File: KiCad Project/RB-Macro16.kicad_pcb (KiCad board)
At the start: 2 copper layers, 3.4 x 3 mm, 67 parts, among them J1 USB_C_Receptacle, J2 AVR-ISP-6, K0A1 KEYSW, K0B1 KEYSW, K0C1 KEYSW, K0D1 KEYSW, K1A1 KEYSW, K1B1 KEYSW, K1C1 KEYSW, K1D1 KEYSW, K2A1 KEYSW, K2B1 KEYSW, K2C1 KEYSW, K2D1 KEYSW, K3A1 KEYSW, K3B1 KEYSW, K3C1 KEYSW, K3D1 KEYSW, SW1 SW_PUSH, U1 ATMEGA32U4, U2 CherryMX_LTST-A683CEGBW, X1 XTAL_GND

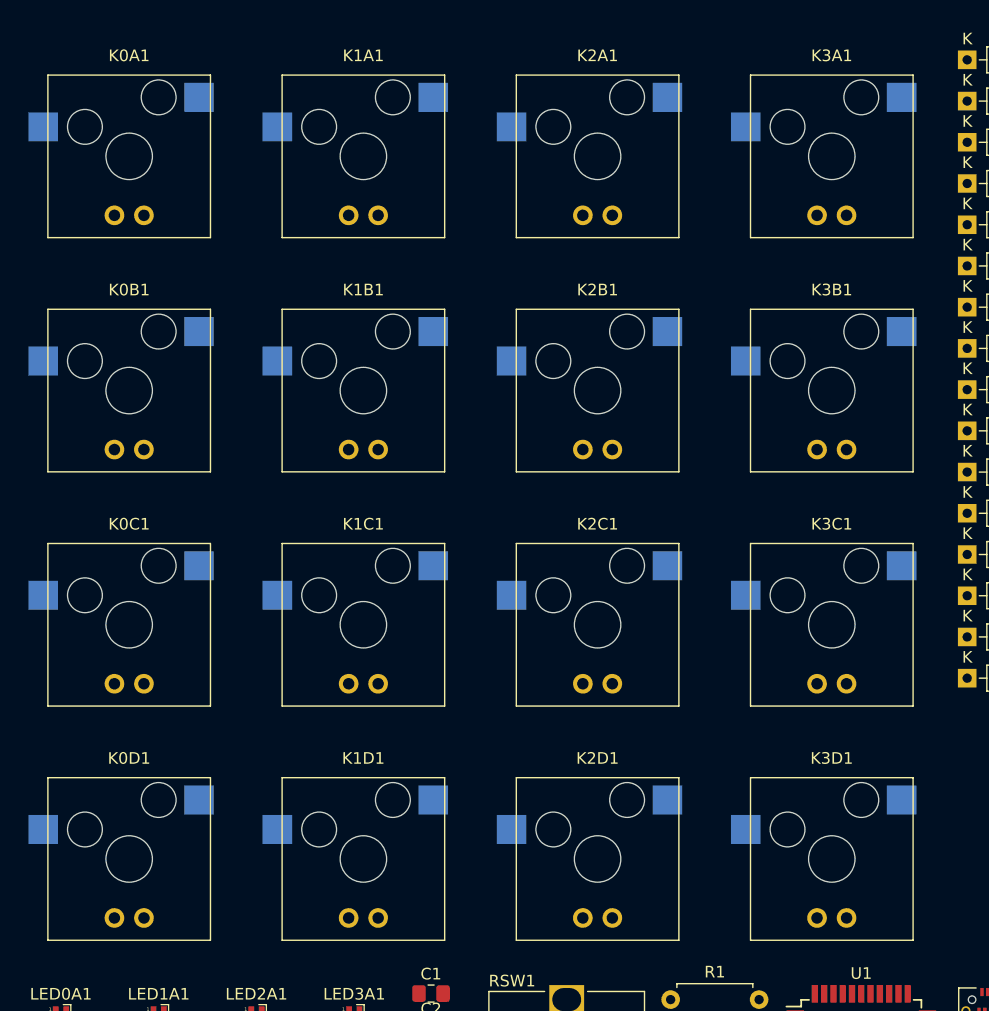
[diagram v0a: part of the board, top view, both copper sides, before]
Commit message: Abandoned New Swtich
Can't find LED new switch footprint uses. Began working on footprint for SK6812MINI-E from Adafruit as a replacement. Added capacitors to LED array and rebuilt it.
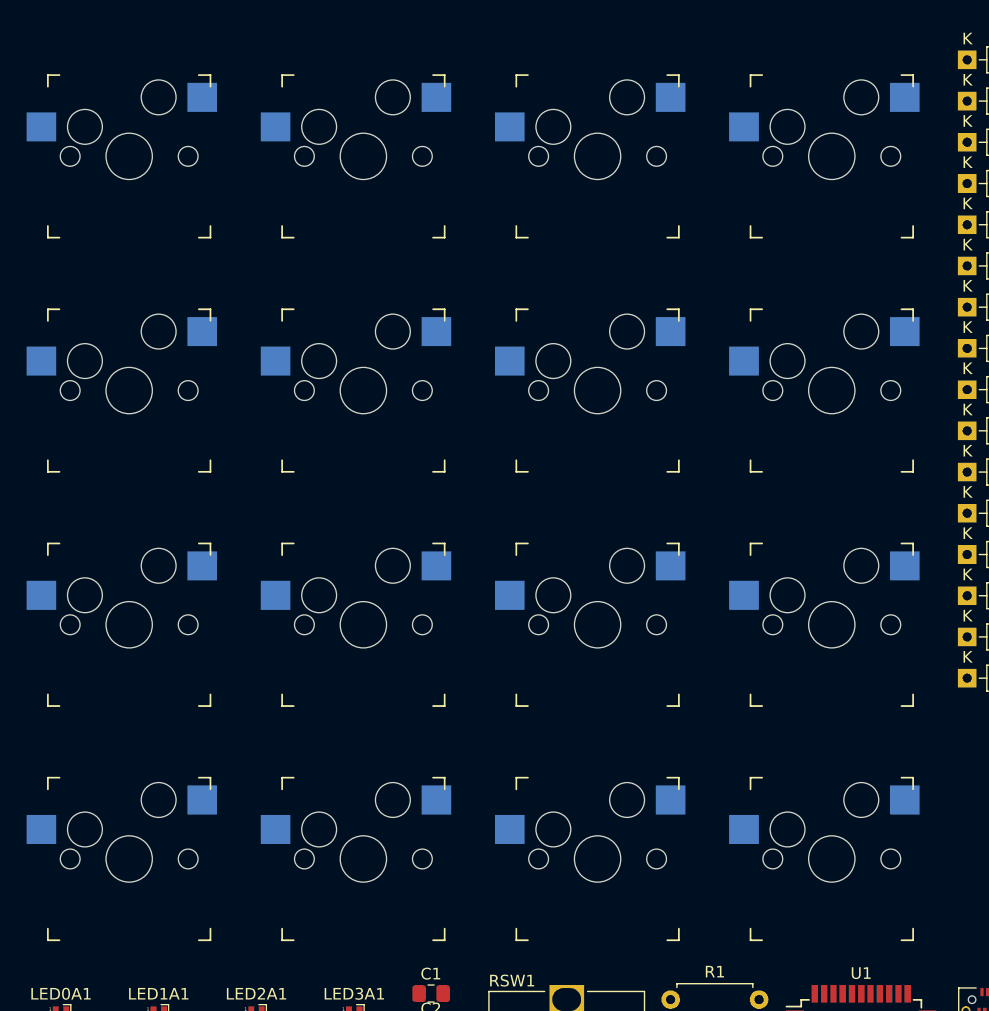
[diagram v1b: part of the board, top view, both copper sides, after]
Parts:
- J2: footprint keyboard_parts:AVR_ICSP_3x2 -> keyboard_parts.pretty-master:AVR_ICSP_3x2
- K0A1, K0B1, K0C1, K0D1, K1A1, K1B1, K1C1, K1D1, K2A1, K2B1, K2C1, K2D1, K3A1, K3B1, K3C1, K3D1: footprint CherryMX_KailhSocket_LED:CherryMX_1.00u_KailhSocket_LED -> keyswitches.pretty-master:Kailh_socket_MX

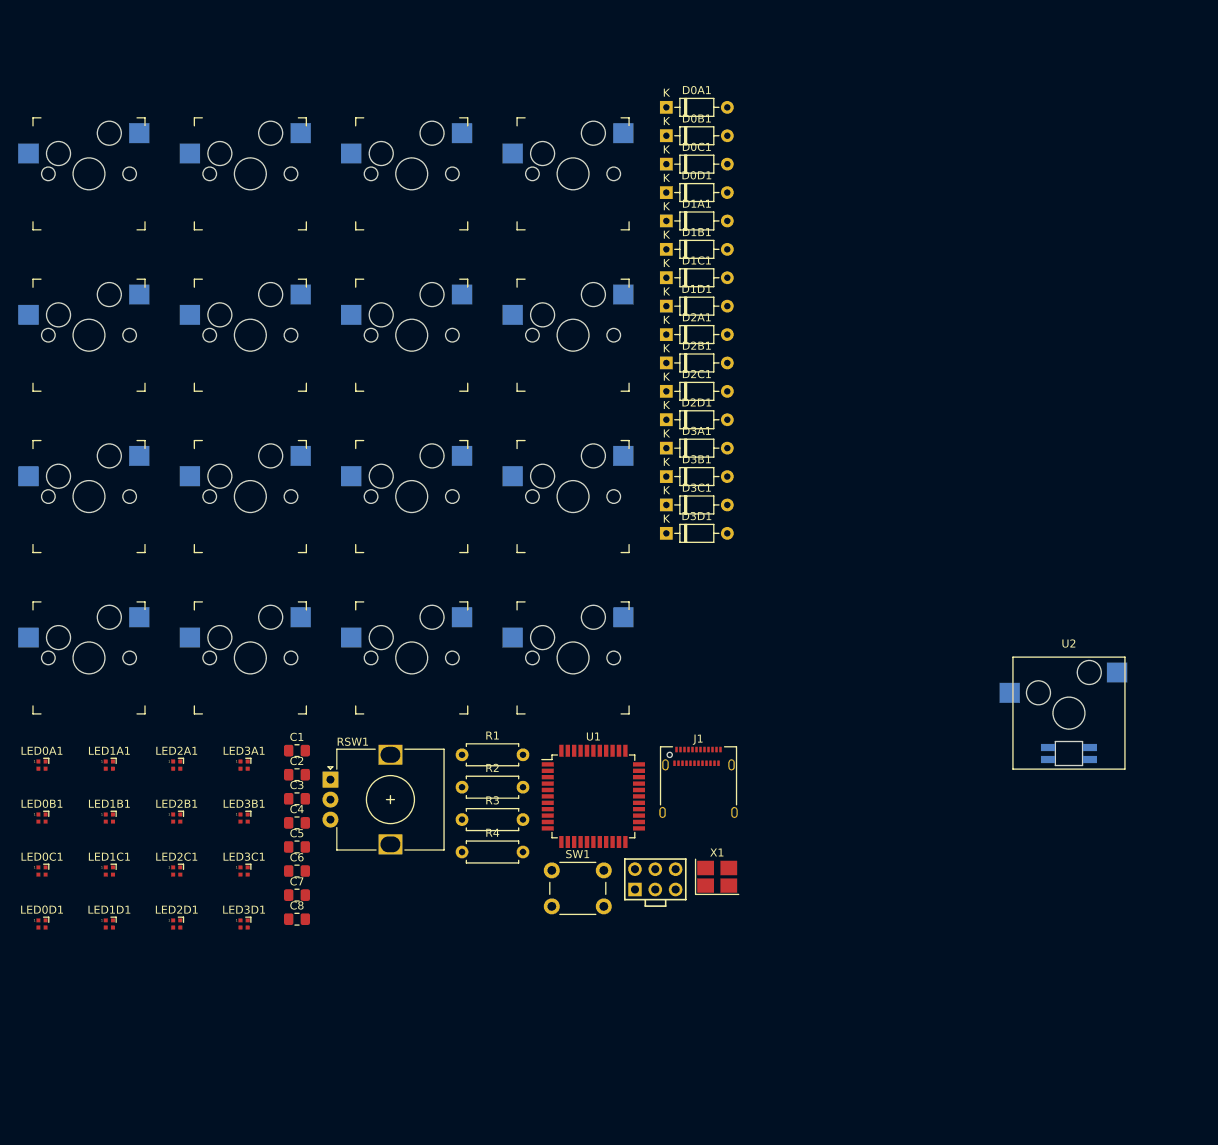
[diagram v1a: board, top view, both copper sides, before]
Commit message: New Switch Symbol and Footprint
Redid switch symbol and footprint to combine hot swap footprint and reverse mount LED footprint. Started work on PCB, laying out switches, diodes, capacitors
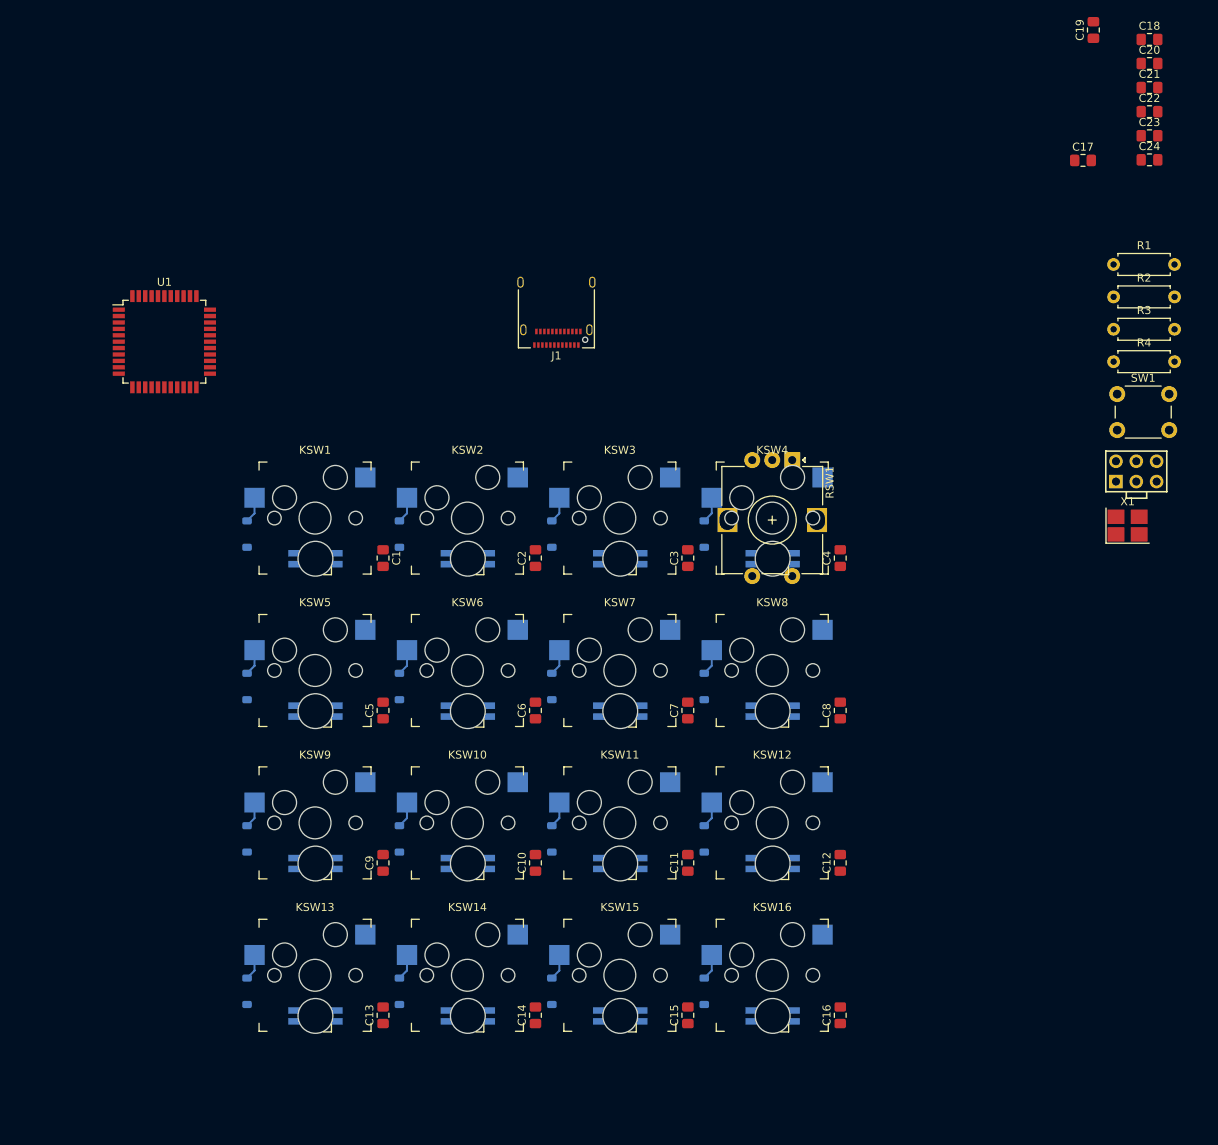
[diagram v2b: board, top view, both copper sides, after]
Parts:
- removed D0A1, D0B1, D0C1, D0D1, D1A1, D1B1, D1C1, D1D1, D2A1, D2B1, D2C1, D2D1, D3A1, D3B1, D3C1, D3D1: D, Diode_THT:D_DO-35_SOD27_P7.62mm_Horizontal
- removed K0A1, K0B1, K0C1, K0D1, K1A1, K1B1, K1C1, K1D1, K2A1, K2B1, K2C1, K2D1, K3A1, K3B1, K3C1, K3D1: KEYSW, keyswitches.pretty-master:Kailh_socket_MX
- removed LED0A1, LED0B1, LED0C1, LED0D1, LED1A1, LED1B1, LED1C1, LED1D1, LED2A1, LED2B1, LED2C1, LED2D1, LED3A1, LED3B1, LED3C1, LED3D1: SK6812, LED_SMD:LED_SK6812_EC15_1.5x1.5mm
- removed U2: CherryMX_LTST-A683CEGBW, CherryMX_KailhSocket_LTST-A683CEGBW:CherryMX_1.00u_KailhSocket_LTST-A683CEGBW
- added C10: C, Capacitor_SMD:C_0805_2012Metric_Pad1.18x1.45mm_HandSolder, F.Cu at (103.4, 132.3)
- added C11: C, Capacitor_SMD:C_0805_2012Metric_Pad1.18x1.45mm_HandSolder, F.Cu at (122.5, 132.3)
- added C12: C, Capacitor_SMD:C_0805_2012Metric_Pad1.18x1.45mm_HandSolder, F.Cu at (141.5, 132.3)
- added C13: C, Capacitor_SMD:C_0805_2012Metric_Pad1.18x1.45mm_HandSolder, F.Cu at (84.4, 151.3)
- added C14: C, Capacitor_SMD:C_0805_2012Metric_Pad1.18x1.45mm_HandSolder, F.Cu at (103.4, 151.3)
- added C15: C, Capacitor_SMD:C_0805_2012Metric_Pad1.18x1.45mm_HandSolder, F.Cu at (122.5, 151.3)
- added C16: C, Capacitor_SMD:C_0805_2012Metric_Pad1.18x1.45mm_HandSolder, F.Cu at (141.5, 151.3)
- added C17: 22p, Capacitor_SMD:C_0805_2012Metric_Pad1.18x1.45mm_HandSolder, F.Cu at (171.9, 44.5)
- added C18: 22p, Capacitor_SMD:C_0805_2012Metric_Pad1.18x1.45mm_HandSolder, F.Cu at (180.2, 29.4)
- added C19: 1u, Capacitor_SMD:C_0805_2012Metric_Pad1.18x1.45mm_HandSolder, F.Cu at (173.2, 28.2)
- added C20: 0.1u, Capacitor_SMD:C_0805_2012Metric_Pad1.18x1.45mm_HandSolder, F.Cu at (180.2, 32.4)
- added C21: 0.1u, Capacitor_SMD:C_0805_2012Metric_Pad1.18x1.45mm_HandSolder, F.Cu at (180.2, 35.4)
- added C22: 0.1u, Capacitor_SMD:C_0805_2012Metric_Pad1.18x1.45mm_HandSolder, F.Cu at (180.2, 38.4)
- added C23: 0.1u, Capacitor_SMD:C_0805_2012Metric_Pad1.18x1.45mm_HandSolder, F.Cu at (180.2, 41.4)
- added C24: 4.7u, Capacitor_SMD:C_0805_2012Metric_Pad1.18x1.45mm_HandSolder, F.Cu at (180.2, 44.4)
- added C9: C, Capacitor_SMD:C_0805_2012Metric_Pad1.18x1.45mm_HandSolder, F.Cu at (84.4, 132.3)
- added D1: D, Diode_SMD:D_SOD-123, B.Cu at (67.4, 91.2)
- added D10: D, Diode_SMD:D_SOD-123, B.Cu at (86.4, 129.3)
- added D11: D, Diode_SMD:D_SOD-123, B.Cu at (105.5, 129.3)
- added D12: D, Diode_SMD:D_SOD-123, B.Cu at (124.5, 129.3)
- added D13: D, Diode_SMD:D_SOD-123, B.Cu at (67.4, 148.3)
- added D14: D, Diode_SMD:D_SOD-123, B.Cu at (86.4, 148.3)
- added D15: D, Diode_SMD:D_SOD-123, B.Cu at (105.5, 148.3)
- added D16: D, Diode_SMD:D_SOD-123, B.Cu at (124.5, 148.3)
- added D2: D, Diode_SMD:D_SOD-123, B.Cu at (86.4, 91.2)
- added D3: D, Diode_SMD:D_SOD-123, B.Cu at (105.5, 91.2)
- added D4: D, Diode_SMD:D_SOD-123, B.Cu at (124.5, 91.2)
- added D5: D, Diode_SMD:D_SOD-123, B.Cu at (67.4, 110.2)
- added D6: D, Diode_SMD:D_SOD-123, B.Cu at (86.4, 110.2)
- added D7: D, Diode_SMD:D_SOD-123, B.Cu at (105.5, 110.2)
- added D8: D, Diode_SMD:D_SOD-123, B.Cu at (124.5, 110.2)
- added D9: D, Diode_SMD:D_SOD-123, B.Cu at (67.4, 129.3)
- added KSW1: Kailh_with_SK6812MINI-E, RB_KeyboardParts:Kailh_with_SK6812MINI-E, F.Cu at (75.9, 89.2)
- added KSW10: Kailh_with_SK6812MINI-E, RB_KeyboardParts:Kailh_with_SK6812MINI-E, F.Cu at (94.9, 127.3)
- added KSW11: Kailh_with_SK6812MINI-E, RB_KeyboardParts:Kailh_with_SK6812MINI-E, F.Cu at (114.0, 127.3)
- added KSW12: Kailh_with_SK6812MINI-E, RB_KeyboardParts:Kailh_with_SK6812MINI-E, F.Cu at (133.0, 127.3)
- added KSW13: Kailh_with_SK6812MINI-E, RB_KeyboardParts:Kailh_with_SK6812MINI-E, F.Cu at (75.9, 146.3)
- added KSW14: Kailh_with_SK6812MINI-E, RB_KeyboardParts:Kailh_with_SK6812MINI-E, F.Cu at (94.9, 146.3)
- added KSW15: Kailh_with_SK6812MINI-E, RB_KeyboardParts:Kailh_with_SK6812MINI-E, F.Cu at (114.0, 146.3)
- added KSW16: Kailh_with_SK6812MINI-E, RB_KeyboardParts:Kailh_with_SK6812MINI-E, F.Cu at (133.0, 146.3)
- added KSW2: Kailh_with_SK6812MINI-E, RB_KeyboardParts:Kailh_with_SK6812MINI-E, F.Cu at (94.9, 89.2)
- added KSW3: Kailh_with_SK6812MINI-E, RB_KeyboardParts:Kailh_with_SK6812MINI-E, F.Cu at (114.0, 89.2)
- added KSW4: Kailh_with_SK6812MINI-E, RB_KeyboardParts:Kailh_with_SK6812MINI-E, F.Cu at (133.0, 89.2)
- added KSW5: Kailh_with_SK6812MINI-E, RB_KeyboardParts:Kailh_with_SK6812MINI-E, F.Cu at (75.9, 108.2)
- added KSW6: Kailh_with_SK6812MINI-E, RB_KeyboardParts:Kailh_with_SK6812MINI-E, F.Cu at (94.9, 108.2)
- added KSW7: Kailh_with_SK6812MINI-E, RB_KeyboardParts:Kailh_with_SK6812MINI-E, F.Cu at (114.0, 108.2)
- added KSW8: Kailh_with_SK6812MINI-E, RB_KeyboardParts:Kailh_with_SK6812MINI-E, F.Cu at (133.0, 108.2)
- added KSW9: Kailh_with_SK6812MINI-E, RB_KeyboardParts:Kailh_with_SK6812MINI-E, F.Cu at (75.9, 127.3)
- C1, C2: value 22p -> C
- C3, C4, C5, C6: value 0.1u -> C
- C7: value 4.7u -> C
- C8: value 1u -> C
- RSW1: footprint Rotary_Encoder:RotaryEncoder_Alps_EC12E_Vertical_H20mm -> Rotary_Encoder:RotaryEncoder_Alps_EC12E-Switch_Vertical_H20mm
- moved R1 101.9 mm to (175.7, 57.5)
- moved R2 101.9 mm to (175.7, 61.5)
- moved R3 101.9 mm to (175.7, 65.6)
- moved R4 101.9 mm to (175.7, 69.7)
- moved SW1 92.4 mm to (176.2, 73.7)
- moved J2 78.8 mm to (178.5, 83.4)
- moved U1 78.1 mm to (57.0, 67.2)
- moved C4 75.5 mm to (141.5, 94.2), turned to 90 degrees
- moved C8 72.7 mm to (141.5, 113.2), turned to 90 degrees
- moved RSW1 70.2 mm to (135.5, 82.0), turned to -90 degrees
- moved X1 67.5 mm to (177.4, 90.1)
- moved J1 63.2 mm to (106.0, 62.5), turned to 180 degrees
- moved C3 57.4 mm to (122.5, 94.2), turned to 90 degrees
- moved C7 54.0 mm to (122.5, 113.2), turned to 90 degrees
- moved C2 40.3 mm to (103.4, 94.2), turned to 90 degrees
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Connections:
- C1 pad 1: Net-(U1-XTAL1) -> VCC
- C2 pad 1: Net-(U1-XTAL2) -> VCC
- C8 pad 1: Net-(U1-UCap) -> VCC
- U1 pad 38: /rowD -> /row3
- U1 pad 39: /rowC -> /row2
- U1 pad 40: /rowB -> /row1
- U1 pad 41: /rowA -> /row0
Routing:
- net Net-(D8-A): track 0.00 -> 3.28 mm
- net Net-(D7-A): track 0.00 -> 3.28 mm
- net Net-(D6-A): track 0.00 -> 3.28 mm
- net Net-(D5-A): track 0.00 -> 3.28 mm
- net Net-(D4-A): track 0.00 -> 3.28 mm
- net Net-(D3-A): track 0.00 -> 3.28 mm
- net Net-(D2-A): track 0.00 -> 3.28 mm
- net Net-(D1-A): track 0.00 -> 3.28 mm
- net Net-(D9-A): track 0.00 -> 3.28 mm
- net Net-(D12-A): track 0.00 -> 3.28 mm
- net Net-(D11-A): track 0.00 -> 3.28 mm
- net Net-(D10-A): track 0.00 -> 3.28 mm
- net Net-(D16-A): track 0.00 -> 3.28 mm
- net Net-(D15-A): track 0.00 -> 3.28 mm
- net Net-(D14-A): track 0.00 -> 3.28 mm
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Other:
- board outline removed

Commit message: Routed PCB
Routed most of the traces in the PCB for the switch block. uP in progress.
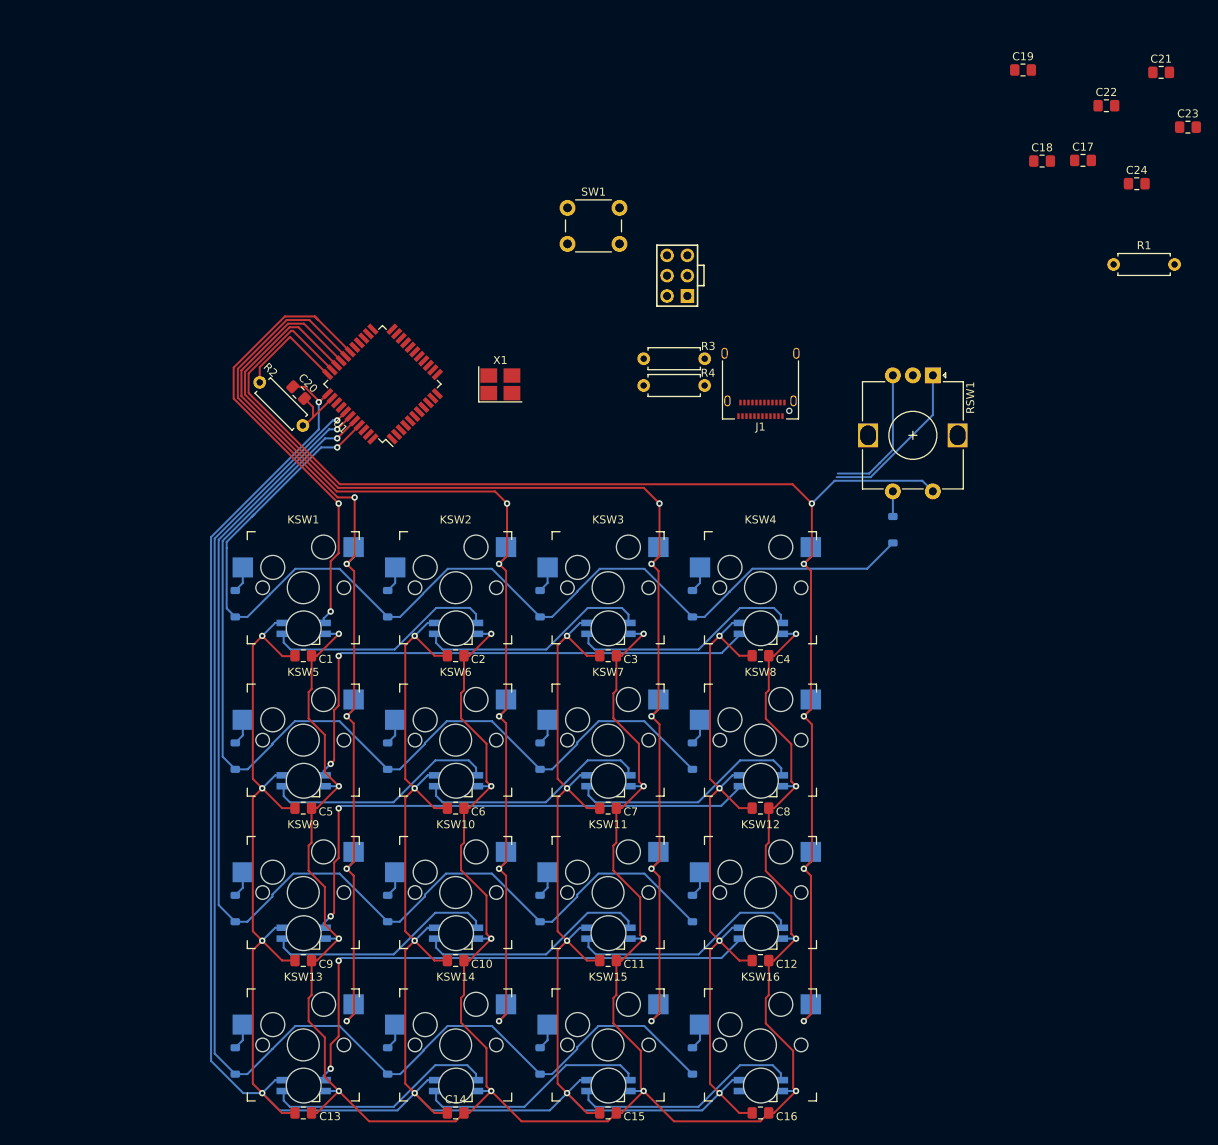
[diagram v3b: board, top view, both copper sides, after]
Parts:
- added D17: D, Diode_SMD:D_SOD-123, B.Cu at (148.1, 90.7)
- D7: value D -> locked
- moved C20 114.0 mm to (73.8, 73.5), turned to -45 degrees
- moved R2 107.3 mm to (69.0, 72.2), turned to -45 degrees
- moved X1 80.4 mm to (99.0, 72.5)
- moved SW1 72.5 mm to (107.4, 50.4)
- moved J2 62.4 mm to (121.2, 58.9), turned to 90 degrees
- moved R3 51.2 mm to (124.6, 69.3), turned to 180 degrees
- moved R4 51.2 mm to (124.6, 72.6), turned to 180 degrees
- moved U1 27.8 mm to (84.3, 72.4), turned to 135 degrees
- moved J1 27.0 mm to (131.6, 71.4)
- moved C18 20.3 mm to (166.8, 44.6)
- moved C10 15.8 mm to (93.5, 144.5), turned to 0 degrees
- moved C14 15.8 mm to (93.5, 163.6), turned to 0 degrees
- moved C2 15.8 mm to (93.5, 106.4), turned to 0 degrees
- moved C6 15.8 mm to (93.5, 125.5), turned to 0 degrees
- moved C1 15.8 mm to (74.4, 106.4), turned to 0 degrees
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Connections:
- RSW1 pad S2: Net-(D4-A) -> Net-(D17-A)
- U1 pad 29: /col3 -> /col0
- U1 pad 30: /col2 -> /col1
- U1 pad 31: /col1 -> /col2
- U1 pad 32: /col0 -> /col3
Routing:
- net VCC: track 0.00 -> 540.3 mm, vias 0 -> 17
- net GND: track 0.00 -> 380.8 mm, vias 0 -> 16
- net /col3: track 0.00 -> 187.4 mm, vias 0 -> 5
- net /row3: track 0.00 -> 163.3 mm, vias 0 -> 1
- net /col2: track 0.00 -> 153.4 mm, vias 0 -> 5
- net /row2: track 0.00 -> 144.0 mm, vias 0 -> 1
- net /col1: track 0.00 -> 136.0 mm, vias 0 -> 5
- net /row0: track 0.00 -> 134.0 mm, vias 0 -> 1
- net /row1: track 0.00 -> 124.3 mm, vias 0 -> 1
- net /col0: track 0.00 -> 119.3 mm, vias 0 -> 5
- net Net-(KSW12-DOUT): track 0.00 -> 67.6 mm, vias 0 -> 2
- net Net-(KSW4-DOUT): track 0.00 -> 67.1 mm, vias 0 -> 2
- net Net-(KSW8-DOUT): track 0.00 -> 67.0 mm, vias 0 -> 2
- net /led0: track 0.00 -> 57.7 mm, vias 0 -> 2
- net Net-(KSW5-DOUT): track 0.00 -> 29.1 mm
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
